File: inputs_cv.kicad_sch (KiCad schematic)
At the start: 41 parts, among them J10 AudioJack2_SwitchT, J11 AudioJack2_SwitchT, J12 AudioJack2_SwitchT, J9 AudioJack2_SwitchT, U33 AD7367-5, U38 OPA4171

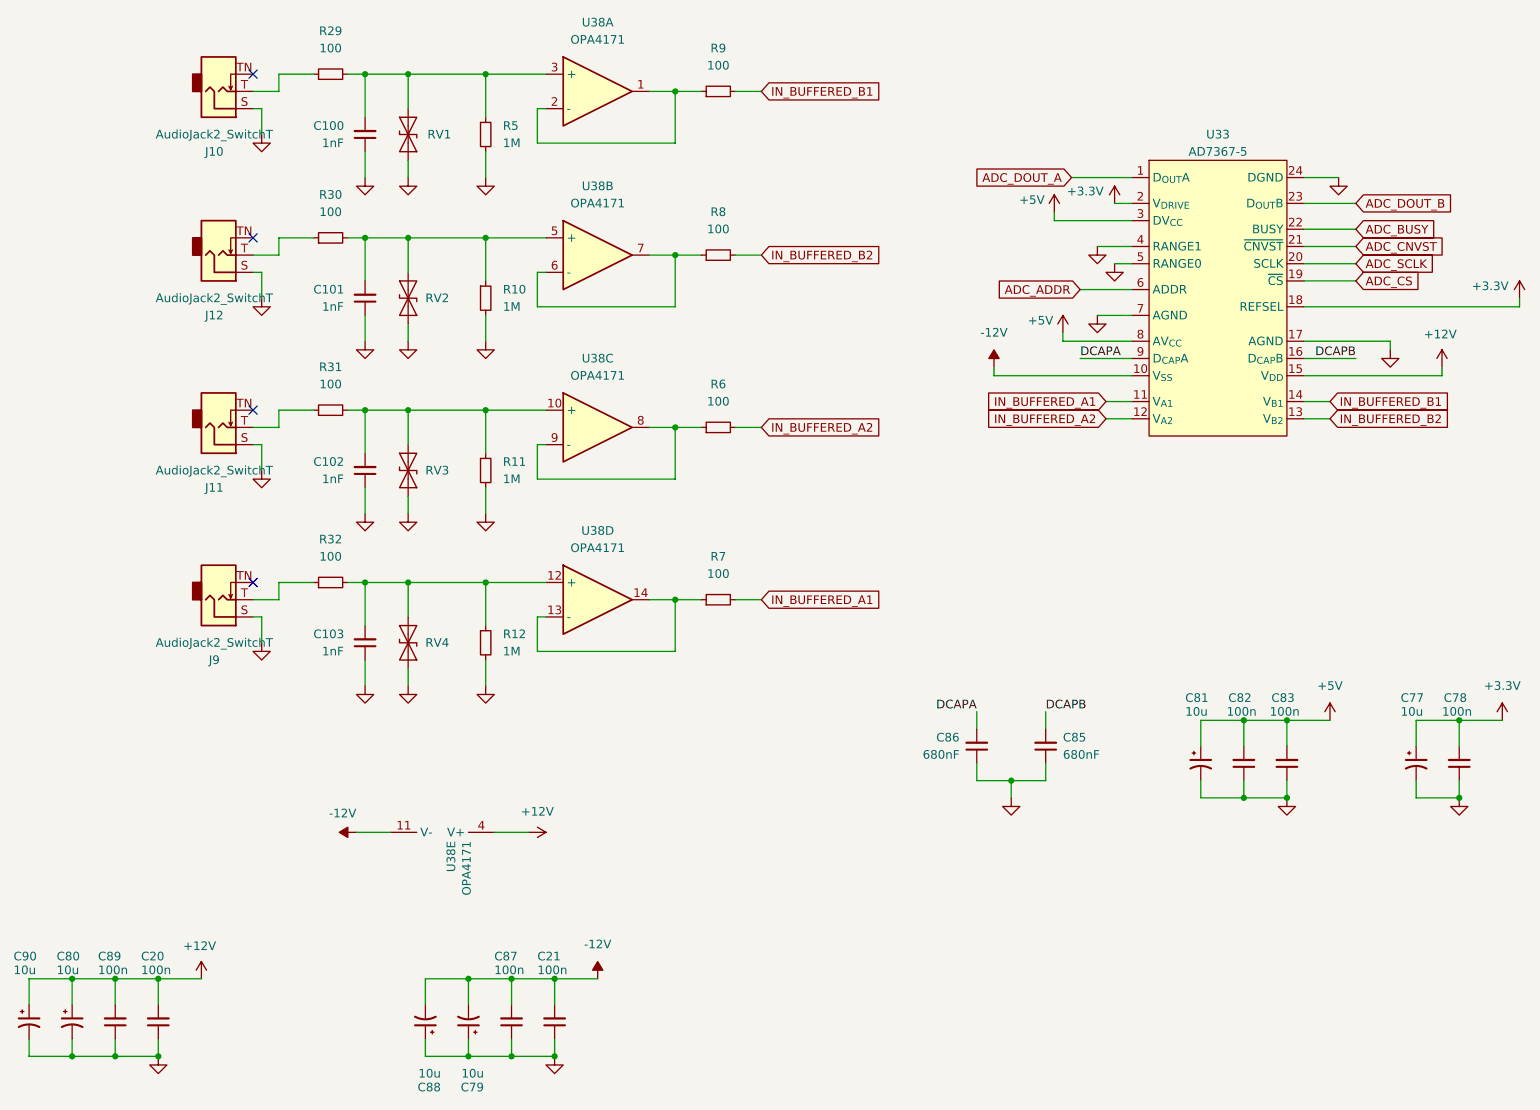
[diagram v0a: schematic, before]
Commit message: RC filters on DAC output
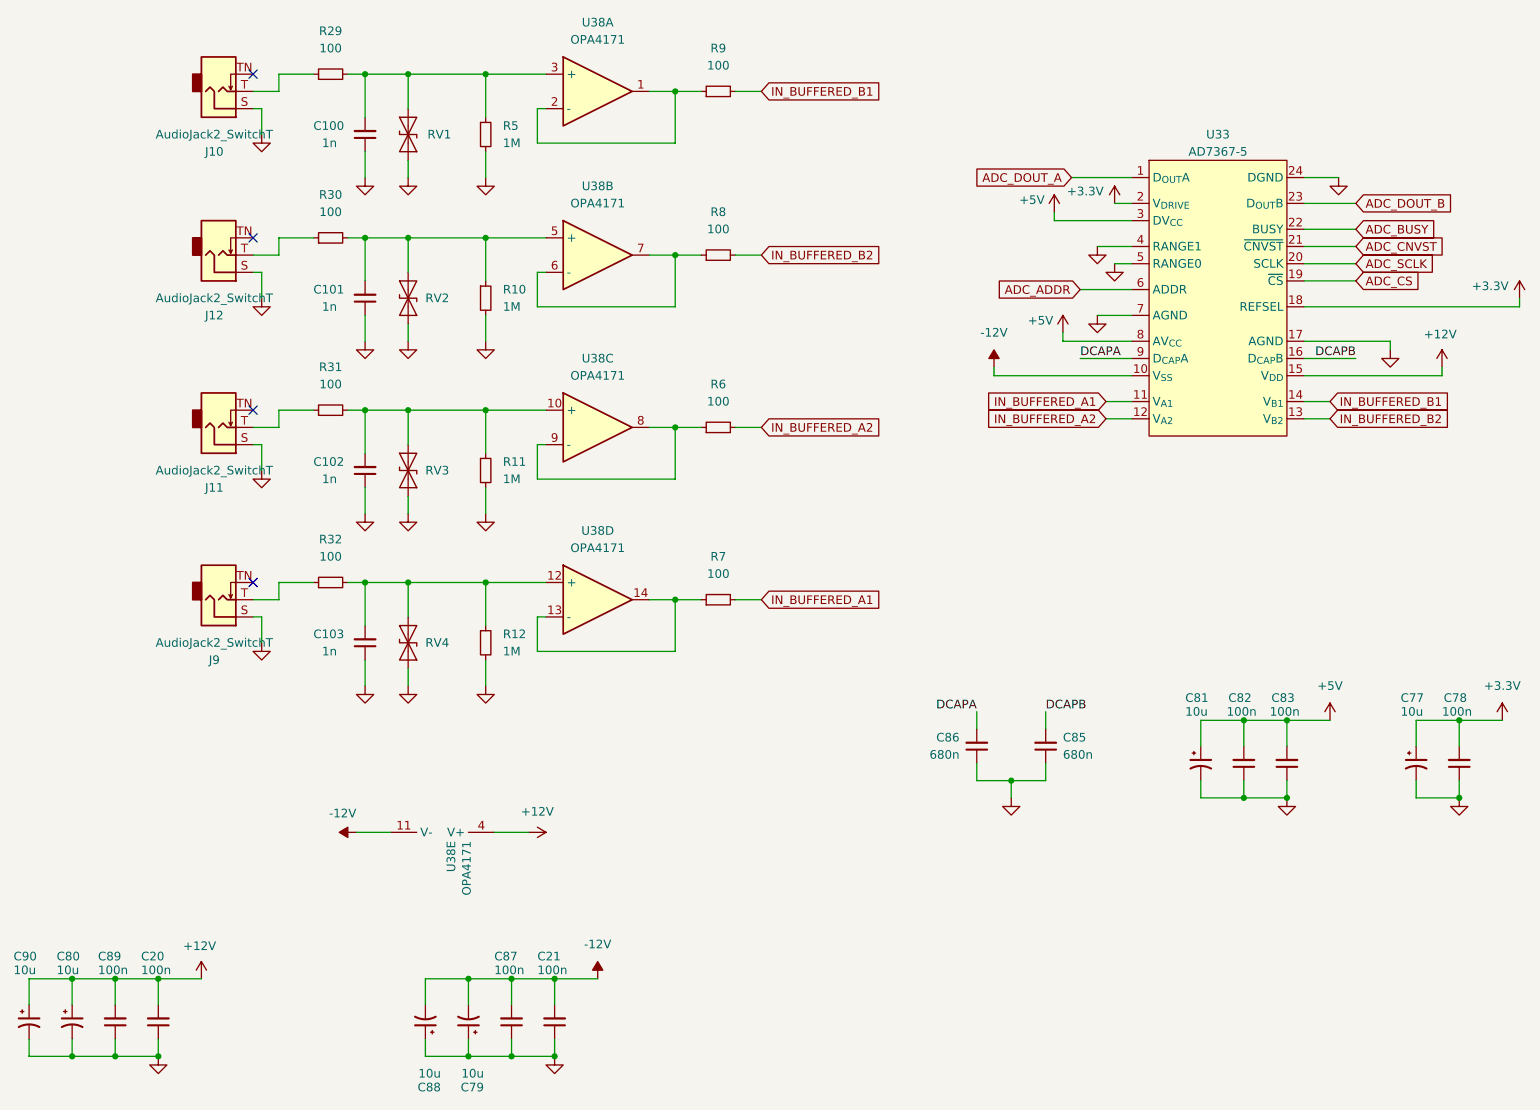
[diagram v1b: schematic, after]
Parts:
- C100, C101, C102, C103: value 1nF -> 1n
- C85, C86: value 680nF -> 680n
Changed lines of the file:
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@@
 			)
 		)
-		(property "Value" "1nF"
+		(property "Value" "1n"
 			(at 86.36 54.61 0)
 			(effects
@@
 			)
 		)
-		(property "Value" "1nF"
+		(property "Value" "1n"
 			(at 86.36 78.74 0)
 			(effects
@@
 			)
 		)
-		(property "Value" "1nF"
+		(property "Value" "1n"
 			(at 86.36 129.54 0)
 			(effects
@@
 			)
 		)
-		(property "Value" "680nF"
+		(property "Value" "680n"
 			(at 195.58 144.7735 0)
 			(effects
@@
 			)
 		)
-		(property "Value" "1nF"
+		(property "Value" "1n"
 			(at 86.36 104.14 0)
 			(effects
@@
 			)
 		)
-		(property "Value" "680nF"
+		(property "Value" "680n"
 			(at 180.34 144.7735 0)
 			(effects

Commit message: v1
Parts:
- C100, C101, C102, C103: value 1n -> 10n; LCSC Part # C1523 -> C15195
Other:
- moved on the sheet: J10, J11, J12, J9
